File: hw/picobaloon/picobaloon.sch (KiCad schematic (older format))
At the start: 45 parts, among them J1 SOLAR+, J2 SWD, J3 DEBUG, J4 GPS_ANT, J5 ANT, J6 SOLAR-, Q1 BC847, Q2 BC857, U1 LMT87DCK, U2 MCP1640CH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

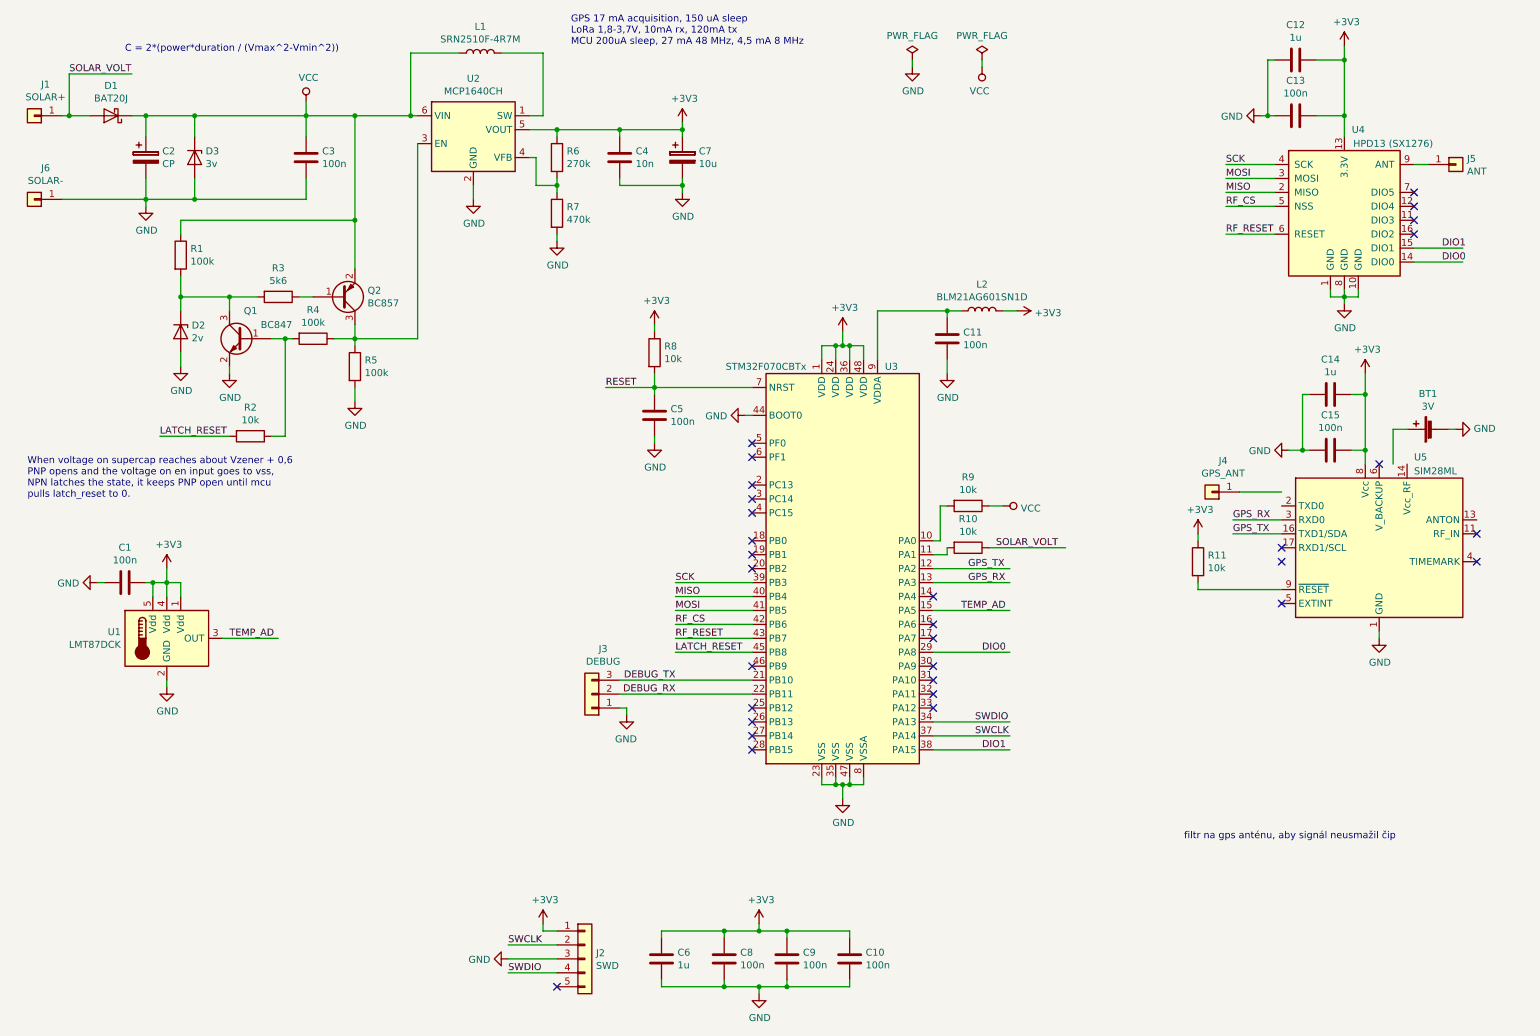
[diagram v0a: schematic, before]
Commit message: HW revision 2 - added pressure sensor
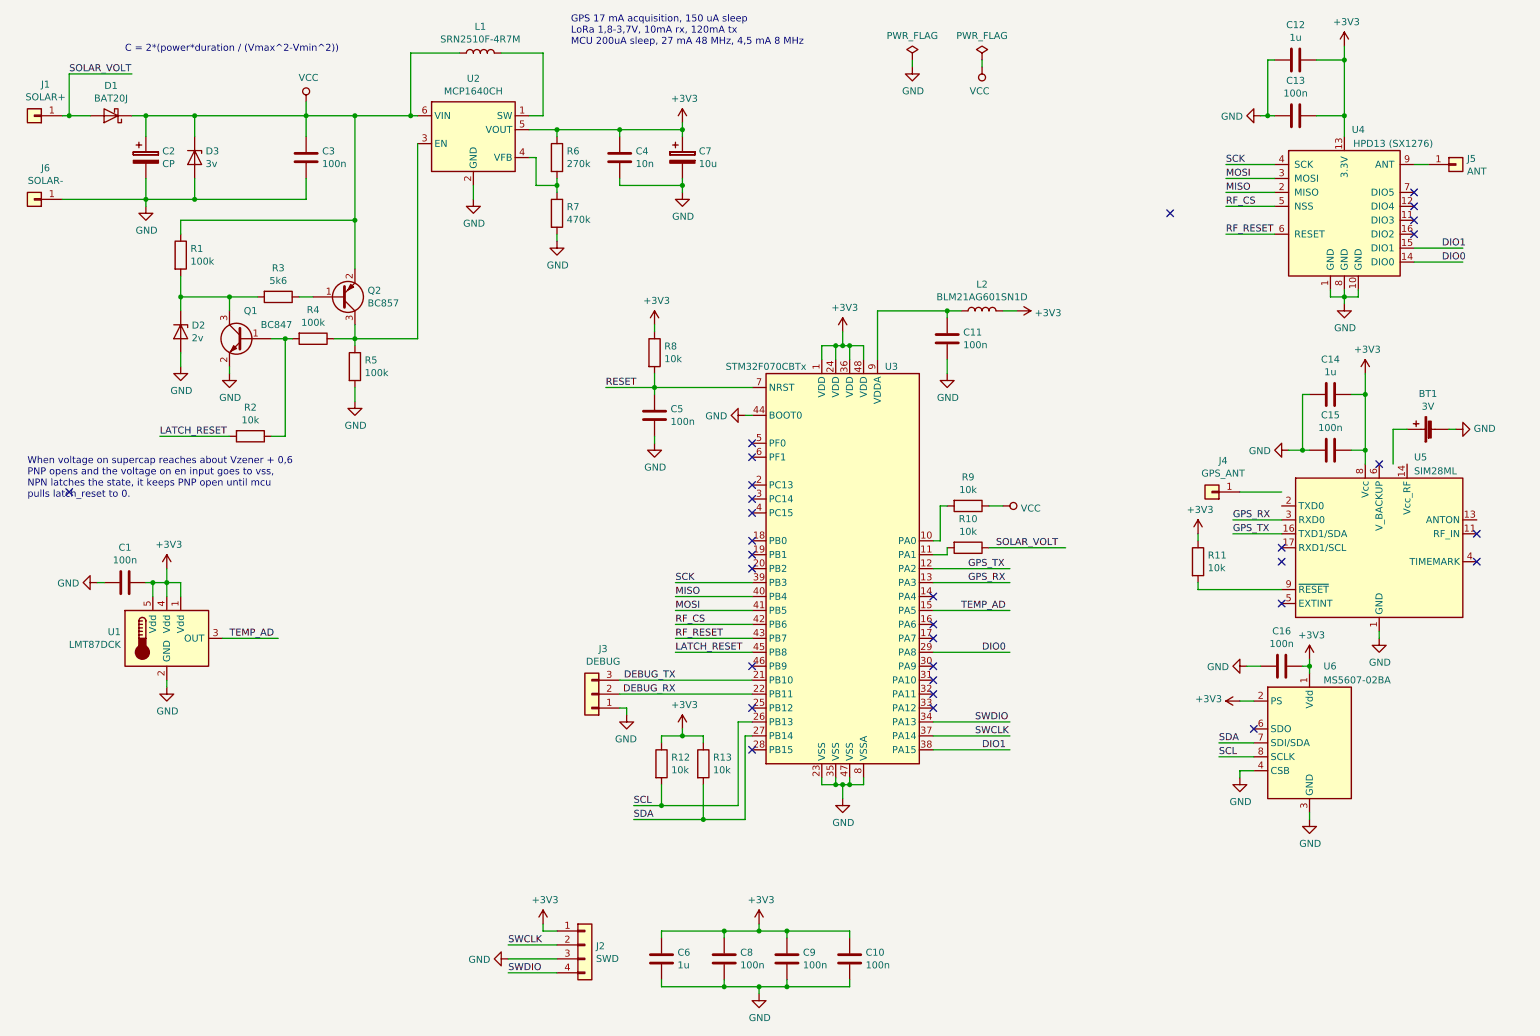
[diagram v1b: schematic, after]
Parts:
- removed J2: SWD, Connector_PinHeader_2.54mm:PinHeader_1x05_P2.54mm_Vertical, symbol Connector_Generic:Conn_01x05
- added C16: 100n, Capacitor_SMD:C_0805_2012Metric, symbol Device:C
- added J2: SWD, Connector_PinHeader_2.54mm:PinHeader_1x04_P2.54mm_Vertical, symbol Connector_Generic:Conn_01x04
- added R12, R13: 10k, Resistor_SMD:R_0805_2012Metric, symbol Device:R
- added U6: MS5607-02BA, Package_LGA:LGA-8_3x5mm_P1.25mm, symbol Sensor:MS5607-02BA
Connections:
- net labels added: SCL, SDA
- wire segments 199 -> 224
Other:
- note removed: "filtr na gps anténu, aby signál neusmažil čip"
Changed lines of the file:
@@
 Title "Deadbadger Picoballoon probe"
 Date ""
-Rev "0.1"
+Rev "0.2"
 Comp "Jakub Kaderka"
 Comment1 "Probe for Hvězdárna a planetárium Brno balloon challange"
@@
 NoConn ~ 10600 1900
 NoConn ~ 10600 1800
-Text Notes 8950 6450 0    50   ~ 0
-filtr na gps anténu, aby signál neusmažil čip
 $Comp
 L Regulator_Switching:MCP1640CH U2
@@
 Text Label 5300 5300 2    50   ~ 0
 DEBUG_TX
-$Comp
-L Connector_Generic:Conn_01x05 J2
-U 1 1 5C67011B
-P 4650 7300
-F 0 "J2" H 4730 7342 50  0000 L CNN
-F 1 "SWD" H 4730 7251 50  0000 L CNN
-F 2 "Connector_PinHeader_2.54mm:PinHeader_1x05_P2.54mm_Vertical" H 4650 7300 50  0001 C CNN
-F 3 "~" H 4650 7300 50  0001 C CNN
-	1    4650 7300
-	1    0    0    -1
-$EndComp
 Wire Wire Line
 	4450 7100 4350 7100
@@
 NoConn ~ 7150 5400
 NoConn ~ 7150 5500
-NoConn ~ 5850 5600
 NoConn ~ 5850 5500
 NoConn ~ 5850 4300
@@
 Wire Wire Line
 	10350 5000 10350 4950
-NoConn ~ 4450 7500
 Wire Wire Line
 	9050 4650 9650 4650
 NoConn ~ 7150 4700
+Text Label 5000 6200 0    50   ~ 0
+SCL
+$Comp
+L Sensor:MS5607-02BA U6
+U 1 1 5C5D4AEB
+P 9850 5750
+F 0 "U6" H 9950 6300 50  0000 L CNN
+F 1 "MS5607-02BA" H 9950 6200 50  0000 L CNN
+F 2 "Package_LGA:LGA-8_3x5mm_P1.25mm" H 9850 5750 50  0001 C CNN
+F 3 "http://www.farnell.com/datasheets/1756127.pdf" H 9850 5750 50  0001 C CNN
+	1    9850 5750
+	1    0    0    -1
+$EndComp
+$Comp
+L power:GND #PWR037
+U 1 1 5C5D4DF8
+P 9850 6300
+F 0 "#PWR037" H 9850 6050 50  0001 C CNN
+F 1 "GND" H 9855 6127 50  0000 C CNN
+F 2 "" H 9850 6300 50  0001 C CNN
+F 3 "" H 9850 6300 50  0001 C CNN
+	1    9850 6300
+	1    0    0    -1
+$EndComp
+Wire Wire Line
+	9850 6300 9850 6250
+$Comp
+L power:+3V3 #PWR036
+U 1 1 5C5F5633
+P 9850 5150
+F 0 "#PWR036" H 9850 5000 50  0001 C CNN
+F 1 "+3V3" H 9865 5323 50  0000 C CNN
+F 2 "" H 9850 5150 50  0001 C CNN
+F 3 "" H 9850 5150 50  0001 C CNN
+	1    9850 5150
+	1    0    0    -1
+$EndComp
+Wire Wire Line
+	9850 5150 9850 5200
+$Comp
+L power:GND #PWR035
+U 1 1 5C600539
+P 9400 5200
+F 0 "#PWR035" H 9400 4950 50  0001 C CNN
+F 1 "GND" V 9405 5072 50  0000 R CNN
+F 2 "" H 9400 5200 50  0001 C CNN
+F 3 "" H 9400 5200 50  0001 C CNN
+	1    9400 5200
+	0    1    1    0
+$EndComp
+$Comp
+L Device:C C16
+U 1 1 5C600628
+P 9650 5200
+F 0 "C16" V 9398 5200 50  0000 C CNN
+F 1 "100n" V 9489 5200 50  0000 C CNN
+F 2 "Capacitor_SMD:C_0805_2012Metric" H 9688 5050 50  0001 C CNN
+F 3 "~" H 9650 5200 50  0001 C CNN
+	1    9650 5200
+	0    1    1    0
+$EndComp
+Wire Wire Line
+	9800 5200 9850 5200
+Connection ~ 9850 5200
+Wire Wire Line
+	9850 5200 9850 5250
+Wire Wire Line
+	9500 5200 9400 5200
+$Comp
+L power:+3V3 #PWR033
+U 1 1 5C616C76
+P 9350 5450
+F 0 "#PWR033" H 9350 5300 50  0001 C CNN
+F 1 "+3V3" V 9365 5578 50  0000 L CNN
+F 2 "" H 9350 5450 50  0001 C CNN
+F 3 "" H 9350 5450 50  0001 C CNN
+	1    9350 5450
+	0    -1   -1   0
+$EndComp
+Wire Wire Line
+	9350 5450 9450 5450
+$Comp
+L power:GND #PWR034
+U 1 1 5C622118
+P 9350 6000
+F 0 "#PWR034" H 9350 5750 50  0001 C CNN
+F 1 "GND" H 9355 5827 50  0000 C CNN
+F 2 "" H 9350 6000 50  0001 C CNN
+F 3 "" H 9350 6000 50  0001 C CNN
+	1    9350 6000
+	1    0    0    -1
+$EndComp
+Wire Wire Line
+	9350 6000 9350 5950
+Wire Wire Line
+	9350 5950 9450 5950
+Wire Wire Line
+	9450 5750 9200 5750
+Text Label 9200 5750 0    50   ~ 0
+SDA
+Wire Wire Line
+	9450 5850 9200 5850
+Text Label 9200 5850 0    50   ~ 0
+SCL
+$Comp
+L Device:R R12
+U 1 1 5C65C0DC
+P 5200 5900
+F 0 "R12" H 5270 5946 50  0000 L CNN
+F 1 "10k" H 5270 5855 50  0000 L CNN
+F 2 "Resistor_SMD:R_0805_2012Metric" V 5130 5900 50  0001 C CNN
+F 3 "~" H 5200 5900 50  0001 C CNN
+	1    5200 5900
+	1    0    0    -1
+$EndComp
+$Comp
+L Device:R R13
+U 1 1 5C65C1BB
+P 5500 5900
+F 0 "R13" H 5570 5946 50  0000 L CNN
+F 1 "10k" H 5570 5855 50  0000 L CNN
+F 2 "Resistor_SMD:R_0805_2012Metric" V 5430 5900 50  0001 C CNN
+F 3 "~" H 5500 5900 50  0001 C CNN
+	1    5500 5900
+	1    0    0    -1
+$EndComp
+$Comp
+L power:+3V3 #PWR031
+U 1 1 5C6736F9
+P 5350 5650
+F 0 "#PWR031" H 5350 5500 50  0001 C CNN
+F 1 "+3V3" H 5365 5823 50  0000 C CNN
+F 2 "" H 5350 5650 50  0001 C CNN
+F 3 "" H 5350 5650 50  0001 C CNN
+	1    5350 5650
+	1    0    0    -1
+$EndComp
+Wire Wire Line
+	5500 5750 5500 5700
+Wire Wire Line
+	5500 5700 5350 5700
+Wire Wire Line
+	5200 5700 5200 5750
+Wire Wire Line
+	5350 5700 5350 5650
+Connection ~ 5350 5700
+Wire Wire Line
+	5350 5700 5200 5700
+Wire Wire Line
+	5200 6200 5200 6050
+Connection ~ 5200 6200
+Wire Wire Line
+	5200 6200 5000 6200
+Wire Wire Line
+	5500 6300 5500 6050
+Wire Wire Line
+	5200 6200 5750 6200
+Wire Wire Line
+	5800 6300 5500 6300
+NoConn ~ 9450 5650
+NoConn ~ 8850 1950
+NoConn ~ 950  3950
+$Comp
+L Connector_Generic:Conn_01x04 J2
+U 1 1 5C700548
+P 4650 7200
+F 0 "J2" H 4730 7192 50  0000 L CNN
+F 1 "SWD" H 4730 7101 50  0000 L CNN
+F 2 "Connector_PinHeader_2.54mm:PinHeader_1x04_P2.54mm_Vertical" H 4650 7200 50  0001 C CNN
+F 3 "~" H 4650 7200 50  0001 C CNN
+	1    4650 7200
+	1    0    0    -1
+$EndComp
+Wire Wire Line
+	5000 6300 5500 6300
+Connection ~ 5500 6300
+Wire Wire Line
+	5750 5600 5850 5600
+Wire Wire Line
+	5750 5600 5750 6200
+Wire Wire Line
+	5850 5700 5800 5700
+Wire Wire Line
+	5800 5700 5800 6300
 NoConn ~ 5850 5800
-NoConn ~ 5850 5700
+Text Label 5000 6300 0    50   ~ 0
+SDA
 $EndSCHEMATC

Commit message: HW revision 3. Added resistors for simple esd protection
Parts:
- added R14, R15: 1M, Resistor_SMD:R_0805_2012Metric, symbol Device:R
- C2: value CP -> 3F/3V
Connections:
- wire segments 224 -> 230
- no-connect marks 31 -> 29
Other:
- note added: "Resistor on antennas are added as a simple ESD\nprotection as the air in high altitudes is dry\nand some charge might build up"
- moved on the sheet: BT1, C1, C12, C13, C14, C15, C16, D3, J4, J5, R11, U1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

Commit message: Updated schematic to match the final symbol in the official repo
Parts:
- removed U6: MS5607-02BA, Package_LGA:LGA-8_3x5mm_P1.25mm, symbol Sensor:MS5607-02BA
- added U6: MS5607-02BA, Package_LGA:LGA-8_3x5mm_P1.25mm, symbol Sensor_Pressure:MS5607-02BA
- C2: value 3F/3V -> 3F3/3V
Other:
- moved on the sheet: BT1, C14, C15, C16, J4, R11, R14, U5
